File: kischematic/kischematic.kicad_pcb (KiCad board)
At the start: 2 copper layers, 26.7 x 50 mm, 105 parts, among them IC1 BlueNRG, IC10 128x64OLED, IC11 BALF-BRG-01D3, IC2 EFM32ZG108, IC3 BQ297xx, IC4 AAT3672IWO-4.2-1, IC5 TPS6223xx, IC6 APDS-9303, IC7 APDS-9303, IC8 BSD840NH6327XTSA1, IC9 MMA8653FC, J1 0, J2 Screw_Terminal_1x01, J5 Screw_Terminal_1x01, J6 Screw_Terminal_1x01, P1 CONN_01X01, P2 CONN_01X01, P3 CONN_01X01, P4 CONN_01X01, P5 CONN_01X01, P6 CONN_01X01, P7 CONN_01X01, P8 CONN_01X04, P9 CONN_01X04, SW1 SW_Push, SW2 SW_Push, U1 USB-C, U2 SWD_SPRING, U3 FT200XD, Y1 32k, Y2 16M

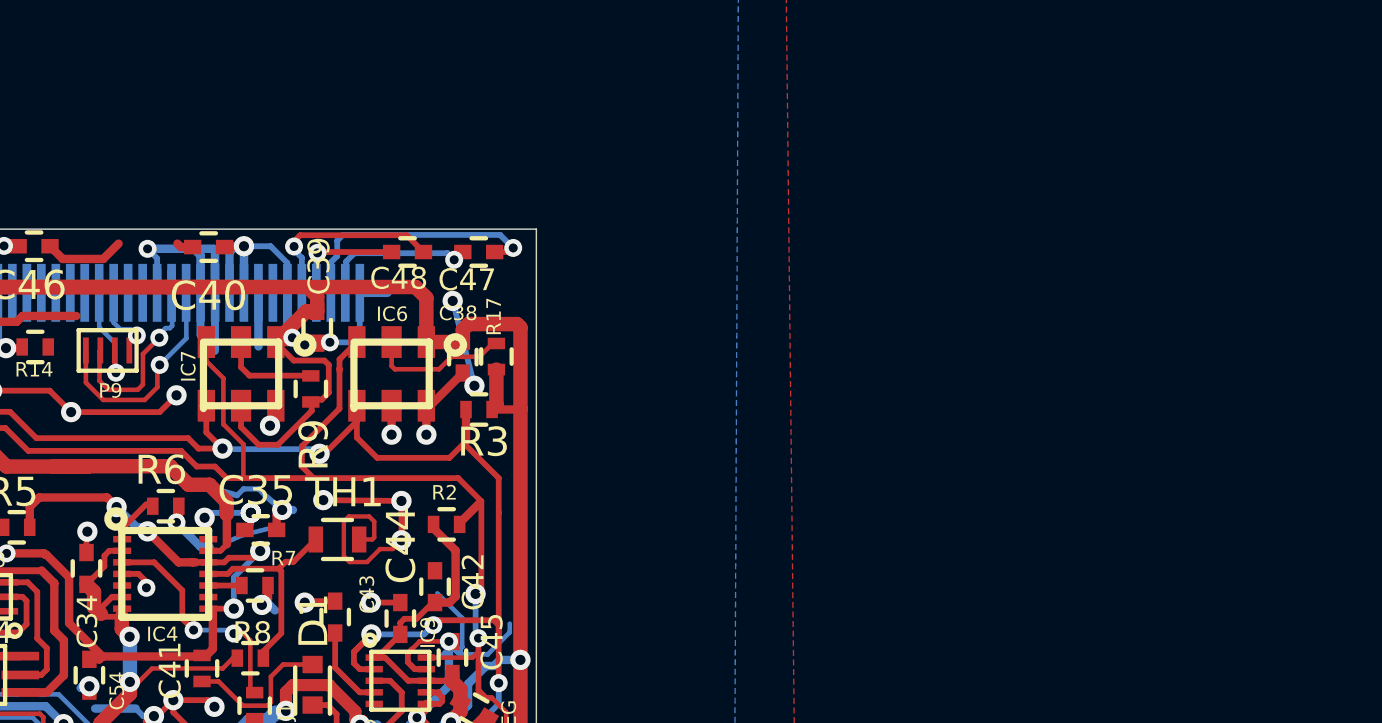
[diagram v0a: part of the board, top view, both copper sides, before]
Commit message: Some initial work on using better light sensors.
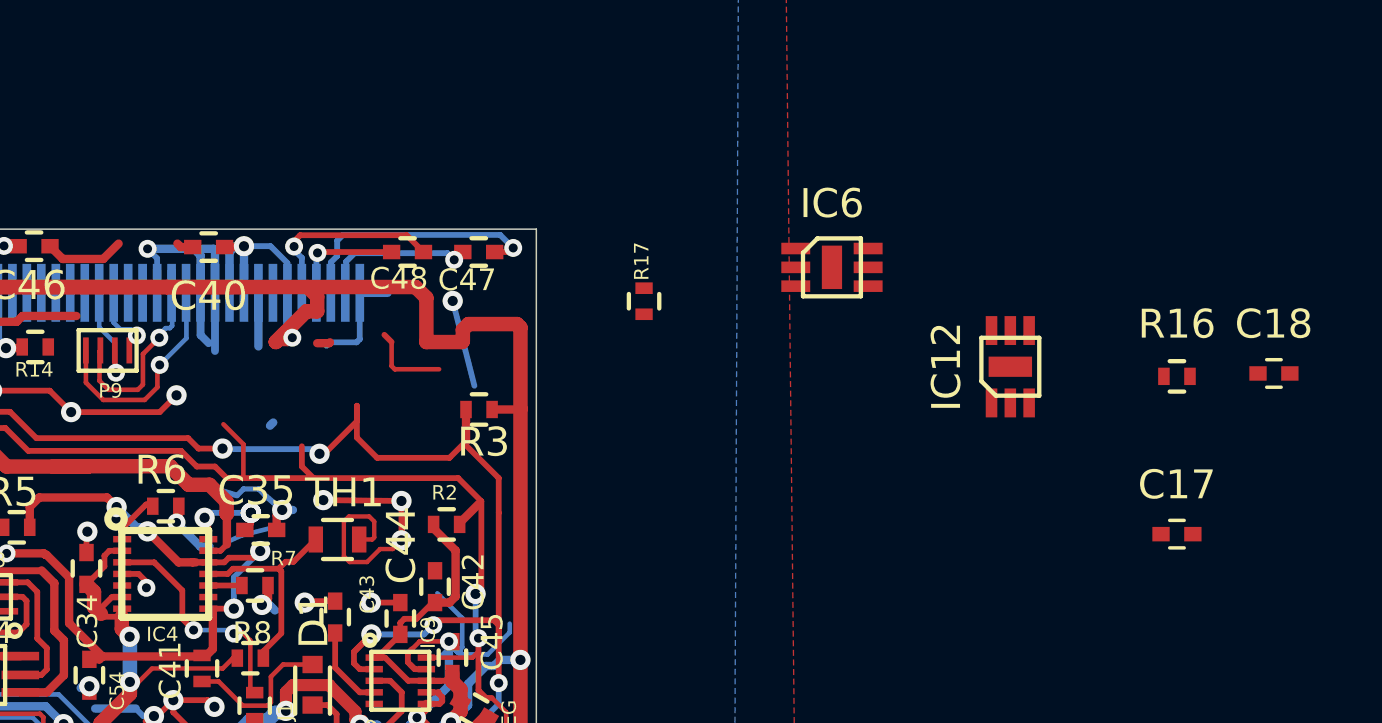
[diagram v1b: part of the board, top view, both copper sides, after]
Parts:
- removed C38, C39: u1, Capacitors_SMD:C_0402
- removed IC7: APDS-9303, newlightmeter:APDS-9303
- removed R9: 91k, Resistors_SMD:R_0402
- added C17: u1, Capacitors_SMD:C_0402, F.Cu at (124.8, 35.5)
- added C18: u1, Capacitors_SMD:C_0402, F.Cu at (128.2, 30.0)
- added IC12: MAX44009, newlightmeter:MAX44009, F.Cu at (119.1, 29.8)
- added R16: 10k, Resistors_SMD:R_0402, F.Cu at (124.8, 30.1)
- IC6: value APDS-9303 -> MAX44009; footprint newlightmeter:APDS-9303 -> newlightmeter:MAX44009
- R17: value 91k -> 10k
- moved IC6 15.6 mm to (112.9, 26.3)
- moved R17 5.45 mm to (106.4, 27.5)
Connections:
- IC6 pad 4: I2C_SCL -> Net-(IC6-Pad4)
- IC6 pad 5: I2C_SDA -> I2C_SCL
- IC6 pad 6: Net-(IC6-Pad6) -> I2C_SDA
- R17 pad 1: VREG -> Net-(IC12-Pad4)
- R17 pad 2: Net-(IC6-Pad6) -> VREG
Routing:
- net VREG: track 201.1 -> 191.2 mm
- net I2C_SDA: track 55.1 -> 47.4 mm
- net GND: track 423.1 -> 417.7 mm, vias 153 -> 147
- net Net-(IC6-Pad6): track 5.23 -> 0.00 mm
- net Net-(IC7-Pad6): track 3.40 -> 0.00 mm
- net (no net): track 3.58 -> 6.76 mm, vias 0 -> 1
- net I2C_SCL: track 54.5 -> 52.4 mm

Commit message: Minor.
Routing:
- net GND: track 417.7 -> 414.4 mm
- net (no net): track 6.76 -> 10.1 mm
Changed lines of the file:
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@@
   (general
     (links 265)
-    (no_connects 24)
+    (no_connects 27)
     (area 75.974999 24.974999 102.725001 75.025001)
     (thickness 1.6)
@@
     (add_net VUSB)
   )
+  (module newlightmeter:MAX44009 (layer F.Cu)
+    (at 119.071713 29.752981)
+    (attr smd)
+    (fp_text reference IC12 (at -2.2 0 90) (layer F.SilkS)
+      (effects (font (size 1 1) (thickness 0.15)))
+    )
+    (fp_text value MAX44009 (at 0 3.55) (layer F.Fab)
+      (effects (font (size 1 1) (thickness 0.15)))
+    )
+    (fp_line (start -0.5 1) (end -1 0.5) (layer F.SilkS) (width 0.15))
+    (fp_line (start -1 0.5) (end -1 -1) (layer F.SilkS) (width 0.15))
+    (fp_line (start -1 -1) (end 1 -1) (layer F.SilkS) (width 0.15))
+    (fp_line (start 1 -1) (end 1 1) (layer F.SilkS) (width 0.15))
+    (fp_line (start 1 1) (end -0.5 1) (layer F.SilkS) (width 0.15))
+    (fp_line (start -1.4 -2.2) (end 1.4 -2.2) (layer F.CrtYd) (width 0.05))
+    (fp_line (start 1.4 -2.2) (end 1.4 2.2) (layer F.CrtYd) (width 0.05))
+    (fp_line (start 1.4 2.2) (end -1.4 2.2) (layer F.CrtYd) (width 0.05))
+    (fp_line (start -1.4 2.2) (end -1.4 -2.2) (layer F.CrtYd) (width 0.05))
+    (pad 6 smd rect (at -0.65 -1.1) (size 0.4 0.75) (layers F.Cu F.Paste F.Mask)
+      (net 27 I2C_SDA) (solder_mask_margin 0.05))
+    (pad 1 smd rect (at -0.65 1.1) (size 0.4 0.75) (layers F.Cu F.Paste F.Mask)
+      (net 2 VREG) (solder_mask_margin 0.05))
+    (pad 5 smd rect (at 0 -1.1) (size 0.4 0.75) (layers F.Cu F.Paste F.Mask)
+      (net 28 I2C_SCL) (solder_mask_margin 0.05))
+    (pad 2 smd rect (at 0 1.1) (size 0.4 0.75) (layers F.Cu F.Paste F.Mask)
+      (net 1 GND) (solder_mask_margin 0.05))
+    (pad 4 smd rect (at 0.65 -1.1) (size 0.4 0.75) (layers F.Cu F.Paste F.Mask)
+      (net 107 "Net-(IC12-Pad4)") (solder_mask_margin 0.05))
+    (pad 3 smd rect (at 0.65 1.1) (size 0.4 0.75) (layers F.Cu F.Paste F.Mask)
+      (net 2 VREG) (solder_mask_margin 0.05))
+    (pad 7 smd rect (at 0 0) (size 1.5 0.7) (layers F.Cu F.Paste F.Mask)
+      (net 1 GND) (solder_mask_margin 0.1))
+  )
+  (module newlightmeter:MAX44009 (layer F.Cu)
+    (at 112.91 26.32 270)
+    (attr smd)
+    (fp_text reference IC6 (at -2.2 0 360) (layer F.SilkS)
+      (effects (font (size 1 1) (thickness 0.15)))
+    )
+    (fp_text value MAX44009 (at 0 3.55 270) (layer F.Fab)
+      (effects (font (size 1 1) (thickness 0.15)))
+    )
+    (fp_line (start -0.5 1) (end -1 0.5) (layer F.SilkS) (width 0.15))
+    (fp_line (start -1 0.5) (end -1 -1) (layer F.SilkS) (width 0.15))
+    (fp_line (start -1 -1) (end 1 -1) (layer F.SilkS) (width 0.15))
+    (fp_line (start 1 -1) (end 1 1) (layer F.SilkS) (width 0.15))
+    (fp_line (start 1 1) (end -0.5 1) (layer F.SilkS) (width 0.15))
+    (fp_line (start -1.4 -2.2) (end 1.4 -2.2) (layer F.CrtYd) (width 0.05))
+    (fp_line (start 1.4 -2.2) (end 1.4 2.2) (layer F.CrtYd) (width 0.05))
+    (fp_line (start 1.4 2.2) (end -1.4 2.2) (layer F.CrtYd) (width 0.05))
+    (fp_line (start -1.4 2.2) (end -1.4 -2.2) (layer F.CrtYd) (width 0.05))
+    (pad 6 smd rect (at -0.65 -1.1 270) (size 0.4 0.75) (layers F.Cu F.Paste F.Mask)
+      (net 27 I2C_SDA) (solder_mask_margin 0.05))
+    (pad 1 smd rect (at -0.65 1.1 270) (size 0.4 0.75) (layers F.Cu F.Paste F.Mask)
+      (net 2 VREG) (solder_mask_margin 0.05))
+    (pad 5 smd rect (at 0 -1.1 270) (size 0.4 0.75) (layers F.Cu F.Paste F.Mask)
+      (net 28 I2C_SCL) (solder_mask_margin 0.05))
+    (pad 2 smd rect (at 0 1.1 270) (size 0.4 0.75) (layers F.Cu F.Paste F.Mask)
+      (net 1 GND) (solder_mask_margin 0.05))
+    (pad 4 smd rect (at 0.65 -1.1 270) (size 0.4 0.75) (layers F.Cu F.Paste F.Mask)
+      (net 108 "Net-(IC6-Pad4)") (solder_mask_margin 0.05))
+    (pad 3 smd rect (at 0.65 1.1 270) (size 0.4 0.75) (layers F.Cu F.Paste F.Mask)
+      (net 1 GND) (solder_mask_margin 0.05))
+    (pad 7 smd rect (at 0 0 270) (size 1.5 0.7) (layers F.Cu F.Paste F.Mask)
+      (net 1 GND) (solder_mask_margin 0.1))
+  )
   (module Capacitors_SMD:C_0402 (layer F.Cu)
     (at 128.176951 29.98548)
@@
     )
   )
-  (module newlightmeter:MAX44009 (layer F.Cu)
-    (at 112.91 26.32 270)
-    (attr smd)
-    (fp_text reference IC6 (at -2.2 0 360) (layer F.SilkS)
-      (effects (font (size 1 1) (thickness 0.15)))
-    )
-    (fp_text value MAX44009 (at 0 3.55 270) (layer F.Fab)
-      (effects (font (size 1 1) (thickness 0.15)))
-    )
-    (fp_line (start -1.4 2.2) (end -1.4 -2.2) (layer F.CrtYd) (width 0.05))
-    (fp_line (start 1.4 2.2) (end -1.4 2.2) (layer F.CrtYd) (width 0.05))
-    (fp_line (start 1.4 -2.2) (end 1.4 2.2) (layer F.CrtYd) (width 0.05))
-    (fp_line (start -1.4 -2.2) (end 1.4 -2.2) (layer F.CrtYd) (width 0.05))
-    (fp_line (start 1 1) (end -0.5 1) (layer F.SilkS) (width 0.15))
-    (fp_line (start 1 -1) (end 1 1) (layer F.SilkS) (width 0.15))
-    (fp_line (start -1 -1) (end 1 -1) (layer F.SilkS) (width 0.15))
-    (fp_line (start -1 0.5) (end -1 -1) (layer F.SilkS) (width 0.15))
-    (fp_line (start -0.5 1) (end -1 0.5) (layer F.SilkS) (width 0.15))
-    (pad 7 smd rect (at 0 0 270) (size 1.5 0.7) (layers F.Cu F.Paste F.Mask)
-      (net 1 GND) (solder_mask_margin 0.1))
-    (pad 3 smd rect (at 0.65 1.25 270) (size 0.4 1) (layers F.Cu F.Paste F.Mask)
-      (net 1 GND) (solder_mask_margin 0.05))
-    (pad 4 smd rect (at 0.65 -1.25 270) (size 0.4 1) (layers F.Cu F.Paste F.Mask)
-      (net 108 "Net-(IC6-Pad4)") (solder_mask_margin 0.05))
-    (pad 2 smd rect (at 0 1.25 270) (size 0.4 1) (layers F.Cu F.Paste F.Mask)
-      (net 1 GND) (solder_mask_margin 0.05))
-    (pad 5 smd rect (at 0 -1.25 270) (size 0.4 1) (layers F.Cu F.Paste F.Mask)
-      (net 28 I2C_SCL) (solder_mask_margin 0.05))
-    (pad 1 smd rect (at -0.65 1.25 270) (size 0.4 1) (layers F.Cu F.Paste F.Mask)
-      (net 2 VREG) (solder_mask_margin 0.05))
-    (pad 6 smd rect (at -0.65 -1.25 270) (size 0.4 1) (layers F.Cu F.Paste F.Mask)
-      (net 27 I2C_SDA) (solder_mask_margin 0.05))
-  )
-  (module newlightmeter:MAX44009 (layer F.Cu)
-    (at 119.071713 29.752981)
-    (attr smd)
-    (fp_text reference IC12 (at -2.2 0 90) (layer F.SilkS)
-      (effects (font (size 1 1) (thickness 0.15)))
-    )
-    (fp_text value MAX44009 (at 0 3.55) (layer F.Fab)
-      (effects (font (size 1 1) (thickness 0.15)))
-    )
-    (fp_line (start -0.5 1) (end -1 0.5) (layer F.SilkS) (width 0.15))
-    (fp_line (start -1 0.5) (end -1 -1) (layer F.SilkS) (width 0.15))
-    (fp_line (start -1 -1) (end 1 -1) (layer F.SilkS) (width 0.15))
-    (fp_line (start 1 -1) (end 1 1) (layer F.SilkS) (width 0.15))
-    (fp_line (start 1 1) (end -0.5 1) (layer F.SilkS) (width 0.15))
-    (fp_line (start -1.4 -2.2) (end 1.4 -2.2) (layer F.CrtYd) (width 0.05))
-    (fp_line (start 1.4 -2.2) (end 1.4 2.2) (layer F.CrtYd) (width 0.05))
-    (fp_line (start 1.4 2.2) (end -1.4 2.2) (layer F.CrtYd) (width 0.05))
-    (fp_line (start -1.4 2.2) (end -1.4 -2.2) (layer F.CrtYd) (width 0.05))
-    (pad 6 smd rect (at -0.65 -1.25) (size 0.4 1) (layers F.Cu F.Paste F.Mask)
-      (net 27 I2C_SDA) (solder_mask_margin 0.05))
-    (pad 1 smd rect (at -0.65 1.25) (size 0.4 1) (layers F.Cu F.Paste F.Mask)
-      (net 2 VREG) (solder_mask_margin 0.05))
-    (pad 5 smd rect (at 0 -1.25) (size 0.4 1) (layers F.Cu F.Paste F.Mask)
-      (net 28 I2C_SCL) (solder_mask_margin 0.05))
-    (pad 2 smd rect (at 0 1.25) (size 0.4 1) (layers F.Cu F.Paste F.Mask)
-      (net 1 GND) (solder_mask_margin 0.05))
-    (pad 4 smd rect (at 0.65 -1.25) (size 0.4 1) (layers F.Cu F.Paste F.Mask)
-      (net 107 "Net-(IC12-Pad4)") (solder_mask_margin 0.05))
-    (pad 3 smd rect (at 0.65 1.25) (size 0.4 1) (layers F.Cu F.Paste F.Mask)
-      (net 2 VREG) (solder_mask_margin 0.05))
-    (pad 7 smd rect (at 0 0) (size 1.5 0.7) (layers F.Cu F.Paste F.Mask)
-      (net 1 GND) (solder_mask_margin 0.1))
-  )
   (module newlightmeter:BALF-NRG-01D3 (layer F.Cu)
     (at 86.39 64.765 270)
@@
   (via (at 99.81 27.48) (size 0.7) (drill 0.35) (layers F.Cu B.Cu) (net 0))
   (segment (start 93.5 31.79) (end 93.61 31.68) (width 0.29) (layer B.Cu) (net 0))
+  (segment (start 95.13 28.94) (end 95.54 28.94) (width 0.29) (layer F.Cu) (net 0))
+  (segment (start 95.54 28.94) (end 95.57 28.91) (width 0.29) (layer F.Cu) (net 0))
+  (segment (start 97.81 29.84) (end 97.7 29.73) (width 0.16) (layer F.Cu) (net 0))
+  (segment (start 97.7 29.73) (end 97.7 28.9) (width 0.16) (layer F.Cu) (net 0) (status 20))
+  (segment (start 99.34 29.84) (end 97.81 29.84) (width 0.16) (layer F.Cu) (net 0))
+  (segment (start 97.45 28.65) (end 97.7 28.9) (width 0.2) (layer F.Cu) (net 0) (status 30))
   (via (at 97.65 63.37) (size 0.7) (drill 0.35) (layers F.Cu B.Cu) (net 1))
   (segment (start 97.65 63.37) (end 96.65 63.37) (width 0.16) (layer B.Cu) (net 1))
@@
   (segment (start 91.1 25.91) (end 90.87 25.68) (width 0.29) (layer B.Cu) (net 1))
   (segment (start 91.1 27.2) (end 91.1 25.91) (width 0.29) (layer B.Cu) (net 1))
-  (segment (start 95.13 28.94) (end 95.54 28.94) (width 0.29) (layer F.Cu) (net 1))
-  (segment (start 95.54 28.94) (end 95.57 28.91) (width 0.29) (layer F.Cu) (net 1))
   (segment (start 96.6 28.8) (end 96.49 28.91) (width 0.2) (layer B.Cu) (net 1))
   (segment (start 96.49 28.91) (end 95.57 28.91) (width 0.2) (layer B.Cu) (net 1))
@@
   (segment (start 94 47) (end 94.71 46.29) (width 0.2) (layer F.Cu) (net 1) (status 30))
   (segment (start 94 47) (end 95 48) (width 0.2) (layer F.Cu) (net 1) (status 30))
-  (segment (start 97.81 29.84) (end 97.7 29.73) (width 0.16) (layer F.Cu) (net 1))
-  (segment (start 97.7 29.73) (end 97.7 28.9) (width 0.16) (layer F.Cu) (net 1) (status 20))
-  (segment (start 99.34 29.84) (end 97.81 29.84) (width 0.16) (layer F.Cu) (net 1))
-  (segment (start 97.45 28.65) (end 97.7 28.9) (width 0.2) (layer F.Cu) (net 1) (status 30))
   (via (at 94.27 28.75) (size 0.62) (drill 0.31) (layers F.Cu B.Cu) (net 2))
   (segment (start 94.12 28.9) (end 93.7 28.9) (width 0.29) (layer F.Cu) (net 2))

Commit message: Minor.
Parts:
- moved IC6 9.04 mm to (105.1, 30.9), turned to 90 degrees
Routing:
- net (no net): track 10.1 -> 3.73 mm, vias 1 -> 0
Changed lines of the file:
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@@
     (thickness 1.6)
     (drawings 223)
-    (tracks 2156)
+    (tracks 2148)
     (zones 0)
     (modules 105)
@@
   )
   (module newlightmeter:MAX44009 (layer F.Cu)
-    (at 112.91 26.32 270)
+    (at 105.1 30.87 90)
     (attr smd)
-    (fp_text reference IC6 (at -2.2 0 360) (layer F.SilkS)
+    (fp_text reference IC6 (at -2.2 0 180) (layer F.SilkS)
       (effects (font (size 1 1) (thickness 0.15)))
     )
-    (fp_text value MAX44009 (at 0 3.55 270) (layer F.Fab)
+    (fp_text value MAX44009 (at 0 3.55 90) (layer F.Fab)
       (effects (font (size 1 1) (thickness 0.15)))
     )
@@
     (fp_line (start 1.4 2.2) (end -1.4 2.2) (layer F.CrtYd) (width 0.05))
     (fp_line (start -1.4 2.2) (end -1.4 -2.2) (layer F.CrtYd) (width 0.05))
-    (pad 6 smd rect (at -0.65 -1.1 270) (size 0.4 0.75) (layers F.Cu F.Paste F.Mask)
+    (pad 6 smd rect (at -0.65 -1.1 90) (size 0.4 0.75) (layers F.Cu F.Paste F.Mask)
       (net 27 I2C_SDA) (solder_mask_margin 0.05))
-    (pad 1 smd rect (at -0.65 1.1 270) (size 0.4 0.75) (layers F.Cu F.Paste F.Mask)
+    (pad 1 smd rect (at -0.65 1.1 90) (size 0.4 0.75) (layers F.Cu F.Paste F.Mask)
       (net 2 VREG) (solder_mask_margin 0.05))
-    (pad 5 smd rect (at 0 -1.1 270) (size 0.4 0.75) (layers F.Cu F.Paste F.Mask)
+    (pad 5 smd rect (at 0 -1.1 90) (size 0.4 0.75) (layers F.Cu F.Paste F.Mask)
       (net 28 I2C_SCL) (solder_mask_margin 0.05))
-    (pad 2 smd rect (at 0 1.1 270) (size 0.4 0.75) (layers F.Cu F.Paste F.Mask)
+    (pad 2 smd rect (at 0 1.1 90) (size 0.4 0.75) (layers F.Cu F.Paste F.Mask)
       (net 1 GND) (solder_mask_margin 0.05))
-    (pad 4 smd rect (at 0.65 -1.1 270) (size 0.4 0.75) (layers F.Cu F.Paste F.Mask)
+    (pad 4 smd rect (at 0.65 -1.1 90) (size 0.4 0.75) (layers F.Cu F.Paste F.Mask)
       (net 108 "Net-(IC6-Pad4)") (solder_mask_margin 0.05))
-    (pad 3 smd rect (at 0.65 1.1 270) (size 0.4 0.75) (layers F.Cu F.Paste F.Mask)
+    (pad 3 smd rect (at 0.65 1.1 90) (size 0.4 0.75) (layers F.Cu F.Paste F.Mask)
       (net 1 GND) (solder_mask_margin 0.05))
-    (pad 7 smd rect (at 0 0 270) (size 1.5 0.7) (layers F.Cu F.Paste F.Mask)
+    (pad 7 smd rect (at 0 0 90) (size 1.5 0.7) (layers F.Cu F.Paste F.Mask)
       (net 1 GND) (solder_mask_margin 0.1))
   )
@@
   (segment (start 87.3 68.85) (end 87.65 68.85) (width 0.29) (layer B.Cu) (net 0))
   (segment (start 87.29 68.86) (end 87.3 68.85) (width 0.29) (layer B.Cu) (net 0))
-  (segment (start 100.56 30.41) (end 99.81 27.48) (width 0.2) (layer B.Cu) (net 0))
-  (via (at 99.81 27.48) (size 0.7) (drill 0.35) (layers F.Cu B.Cu) (net 0))
   (segment (start 93.5 31.79) (end 93.61 31.68) (width 0.29) (layer B.Cu) (net 0))
-  (segment (start 95.13 28.94) (end 95.54 28.94) (width 0.29) (layer F.Cu) (net 0))
-  (segment (start 95.54 28.94) (end 95.57 28.91) (width 0.29) (layer F.Cu) (net 0))
-  (segment (start 97.81 29.84) (end 97.7 29.73) (width 0.16) (layer F.Cu) (net 0))
-  (segment (start 97.7 29.73) (end 97.7 28.9) (width 0.16) (layer F.Cu) (net 0) (status 20))
-  (segment (start 99.34 29.84) (end 97.81 29.84) (width 0.16) (layer F.Cu) (net 0))
-  (segment (start 97.45 28.65) (end 97.7 28.9) (width 0.2) (layer F.Cu) (net 0) (status 30))
+  (via (at 86.76 40.78) (size 0.7) (drill 0.35) (layers F.Cu B.Cu) (net 1))
+  (segment (start 86.76 40.78) (end 86.94 40.96) (width 0.29) (layer F.Cu) (net 1))
+  (segment (start 86.83 40.85) (end 86.96 40.85) (width 0.29) (layer B.Cu) (net 1))
+  (segment (start 86.94 40.96) (end 87.26 40.96) (width 0.29) (layer F.Cu) (net 1))
+  (segment (start 86.76 40.78) (end 86.83 40.85) (width 0.29) (layer B.Cu) (net 1))
   (via (at 97.65 63.37) (size 0.7) (drill 0.35) (layers F.Cu B.Cu) (net 1))
   (segment (start 97.65 63.37) (end 96.65 63.37) (width 0.16) (layer B.Cu) (net 1))
@@
   (segment (start 85.16 51.77) (end 85.16 52.79) (width 0.16) (layer B.Cu) (net 1))
   (segment (start 85.16 52.79) (end 85.15 52.8) (width 0.16) (layer B.Cu) (net 1))
-  (via (at 87.26 40.79) (size 0.7) (drill 0.35) (layers F.Cu B.Cu) (net 1))
-  (segment (start 87.26 40.79) (end 87.26 40.96) (width 0.29) (layer F.Cu) (net 1))
-  (segment (start 87.26 40.79) (end 87.02 40.79) (width 0.29) (layer B.Cu) (net 1))
-  (segment (start 87.02 40.79) (end 86.96 40.85) (width 0.29) (layer B.Cu) (net 1))
   (via (at 89.49 41.82) (size 0.7) (drill 0.35) (layers F.Cu B.Cu) (net 1))
   (segment (start 88.86 41.56) (end 89.12 41.82) (width 0.2) (layer B.Cu) (net 1))
@@
   (segment (start 93.22 37.98) (end 93.43 37.77) (width 0.29) (layer F.Cu) (net 1))
   (segment (start 93.43 37.77) (end 93.43 37.31) (width 0.29) (layer F.Cu) (net 1) (status 20))
-  (segment (start 95.57 28.91) (end 95.45 29.03) (width 0.2) (layer B.Cu) (net 1))
   (segment (start 93.1 27.2) (end 93.1 29.05) (width 0.29) (layer B.Cu) (net 1) (status 10))
   (segment (start 96.6 27.2) (end 97.56 27.2) (width 0.29) (layer B.Cu) (net 1) (status 10))
@@
   (segment (start 84.15 35.3) (end 83.38 36.07) (width 0.29) (layer F.Cu) (net 32) (status 10))
   (via (at 83.38 36.07) (size 0.62) (drill 0.31) (layers F.Cu B.Cu) (net 32))
+  (segment (start 84.875 41) (end 85.61 41) (width 0.29) (layer F.Cu) (net 33))
+  (segment (start 85.61 41) (end 86.21 40.4) (width 0.29) (layer F.Cu) (net 33))
+  (segment (start 86.21 40.4) (end 86.21 39.26) (width 0.29) (layer F.Cu) (net 33))
+  (segment (start 86.21 39.26) (end 85.88 38.93) (width 0.29) (layer F.Cu) (net 33))
+  (segment (start 85.88 38.93) (end 85.88 37.06) (width 0.29) (layer F.Cu) (net 33))
+  (segment (start 85.88 37.06) (end 85.61 36.79) (width 0.29) (layer F.Cu) (net 33))
   (segment (start 82.16 35.46) (end 82.16 35.34) (width 0.29) (layer F.Cu) (net 33))
   (segment (start 82.16 35.34) (end 83.44 34.06) (width 0.29) (layer F.Cu) (net 33))
-  (segment (start 85.79 41) (end 86.38 40.41) (width 0.29) (layer F.Cu) (net 33))
-  (segment (start 84.875 41) (end 85.79 41) (width 0.29) (layer F.Cu) (net 33) (status 10))
-  (segment (start 86.38 40.41) (end 86.38 39.2) (width 0.29) (layer F.Cu) (net 33))
   (segment (start 82.74 36.81) (end 83.13 37.2) (width 0.29) (layer F.Cu) (net 33) (status 20))
   (segment (start 83.13 37.2) (end 83.2 37.2) (width 0.29) (layer F.Cu) (net 33) (status 30))
@@
   (segment (start 85.6 36.8) (end 83.62 36.8) (width 0.24) (layer F.Cu) (net 33))
   (segment (start 83.62 36.8) (end 83.61 36.79) (width 0.26) (layer F.Cu) (net 33))
-  (segment (start 86.05 37.23) (end 85.61 36.79) (width 0.29) (layer F.Cu) (net 33))
-  (segment (start 86.05 38.87) (end 86.05 37.23) (width 0.29) (layer F.Cu) (net 33))
-  (segment (start 86.38 39.2) (end 86.05 38.87) (width 0.29) (layer F.Cu) (net 33))
   (via (at 86.37 42.1) (size 0.7) (drill 0.35) (layers F.Cu B.Cu) (net 35))
   (segment (start 86.37 42.1) (end 86.4 42.1) (width 0.29) (layer F.Cu) (net 35))
@@
       )
     )
-  )
-  (zone (net 0) (net_name "") (layer F.Cu) (hatch edge 0.508)
-    (connect_pads (clearance 0.18))
-    (min_thickness 0.254)
-    (keepout (tracks allowed) (vias allowed) (copperpour not_allowed))
-    (fill yes (arc_segments 16) (thermal_gap 0.508) (thermal_bridge_width 0.508))
-    (polygon
-      (pts
-        (xy 97.78 30.79) (xy 99.09 30.79) (xy 99.09 31.41) (xy 97.81 31.4) (xy 97.78 30.78)
-      )
-    )
